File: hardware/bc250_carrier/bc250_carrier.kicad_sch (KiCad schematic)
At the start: 15 parts, among them J1 PSU Mini-Fit Jr 2x5, J10 SENSE, J3 STRIP, J5 FAN1 GPIO5, J6 FAN2 GPIO6, J7 FAN3 GPIO7, J8 FAN4 GPIO10, J9 BTN, Q1 2N7000, U1 ESP32-C3 Super Mini

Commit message: hardware: BC-250 carrier rev C — right-angle PSU header, J11 breakout, wider rails
Rev C relays the 80 x 34.5 mm board around a RIGHT-ANGLE Mini-Fit Jr
(DLL-5569-10AW, C22365658) on the bottom edge: the PSU plug lies flat over a
tracks-only "plug zone" and its wires leave over the top edge.  The 3.3 V
strip feed is a 3 mm track, its return 2.5 mm.  New optional 2x8 breakout
header J11 along the left edge carries 3.3V, 5VSB and 12 V on two pins each
plus every unused GPIO (8, 9, 20, 21, 0) with a ground beside it.  The
button J9 grows to 4 pins (12 V + GND for its ring LED), the sense connector
shrinks to a single pin, the fan headers become a 2 x 2 block spaced for real
fan plugs (Ckmtw W-2510S04P, C140769 — C41927 was a shrouded wafer a fan plug
cannot enter), R1 moves to 7.62 mm pitch, GATE hops layers through two vias.

Every LCSC part number was re-verified against LCSC's product API; MOQs and
pin headers (C2337, C124382) fixed.  `make` now runs KiCad's real DRC through
the pcbnew Python module (drc.py; only the two stock-M3-courtyard overlaps are
tolerated) alongside check.py, and `make preview` renders a quick Pillow PNG.

The J11 rails were then widened so the breakout is good for about 2 A each,
not the 1.3-1.6 A its 0.5-0.6 mm tracks allowed: 12 V 1.2 mm (back layer up
the strip between J11 and the module), 5VSB 1.0 mm (front layer, same strip;
its trunk from the header to the module 1.0 -> 1.5 mm since J11's draw flows
through it), 3.3V 0.9 mm — the most that fits between mounting holes H3/H1 and
the board edge under the 0.25 hole / 0.3 edge rules.  The README gains a
current budget: the fan block's split 12 V feed is ~2.7 A per column, enough
for a fan plus an AIO pump.

Still to confirm on hardware: the PSU pin map, the module's orientation, and
fan plug polarity.
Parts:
- removed J10: SENSE, Connector_JST:JST_XH_B2B-XH-A_1x02_P2.50mm_Vertical, symbol Connector_Generic:Conn_01x02
- removed J9: BTN, Connector_JST:JST_XH_B2B-XH-A_1x02_P2.50mm_Vertical, symbol Connector_Generic:Conn_01x02
- added J10: SENSE, Connector_PinHeader_2.54mm:PinHeader_1x01_P2.54mm_Vertical, symbol Connector_Generic:Conn_01x01
- added J11: PWR+GPIO/GND (optional), Connector_PinHeader_2.54mm:PinHeader_2x08_P2.54mm_Vertical, symbol Connector_Generic:Conn_02x08_Odd_Even
- added J9: BUTTON, Connector_JST:JST_XH_B4B-XH-A_1x04_P2.50mm_Vertical, symbol Connector_Generic:Conn_01x04
- J1: value PSU Mini-Fit Jr 2x5 -> PSU Mini-Fit Jr 2x5 R/A; footprint Connector_Molex:Molex_Mini-Fit_Jr_5566-10A_2x05_P4.20mm_Vertical -> Connector_Molex:Molex_Mini-Fit_Jr_5569-10A2_2x05_P4.20mm_Horizontal
- R1: footprint Resistor_THT:R_Axial_DIN0207_L6.3mm_D2.5mm_P10.16mm_Horizontal -> Resistor_THT:R_Axial_DIN0207_L6.3mm_D2.5mm_P7.62mm_Horizontal
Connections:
- net 12V: now also J11.5 (Pin_5), J11.6 (Pin_6), J9.1 (Pin_1)
- net 5VSB: now also J11.3 (Pin_3), J11.4 (Pin_4)
- net BTN: now also J9.3 (Pin_3)
- net GND: now also J11.11 (Pin_11), J11.13 (Pin_13), J11.15 (Pin_15), J11.7 (Pin_7), J11.9 (Pin_9), J9.2 (Pin_2), J9.4 (Pin_4)
- net SENSE: now also J10.1 (Pin_1)
- net GPIO0: now reaches U1.16 (GPIO0)
- net GPIO0: now also J11.16 (Pin_16)
- net GPIO8: now reaches U1.4 (GPIO8)
- net GPIO8: now also J11.8 (Pin_8)
- net GPIO9: now reaches U1.5 (GPIO9)
- net GPIO9: now also J11.10 (Pin_10)
- net GPIO20: now reaches U1.7 (GPIO20)
- net GPIO20: now also J11.12 (Pin_12)
- net GPIO21: now reaches U1.8 (GPIO21)
- net GPIO21: now also J11.14 (Pin_14)
- net VIN renamed 3.3V
- net 3.3V: now also J11.1 (Pin_1), J11.2 (Pin_2)
- no-connect marks 10 -> 5

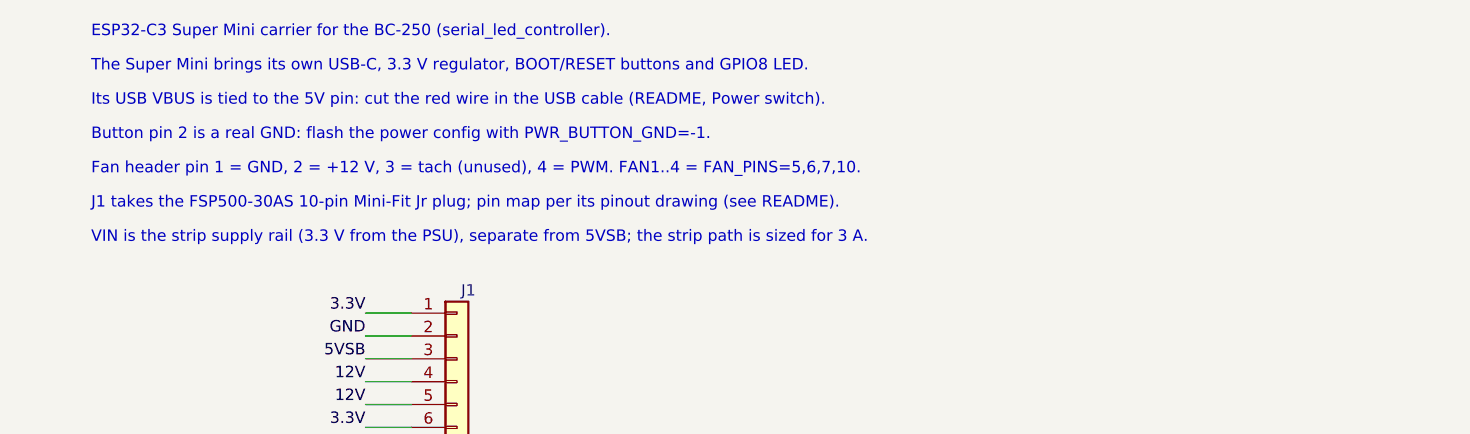
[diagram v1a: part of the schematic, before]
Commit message: hardware: reword two schematic notes that still quoted the retired make variables
The PWR_BUTTON_GND and FAN_PINS variables are gone since v1.18.0/v1.19.0;
the notes now name the config keys (power_switch.pins.button_gnd null,
fans.header1..4 = GPIO 5, 6, 7, 10) and say which J9 pin is the switch
common. Schematic text only — the .kicad_pcb, and so the gerbers already at
the fab, are untouched.
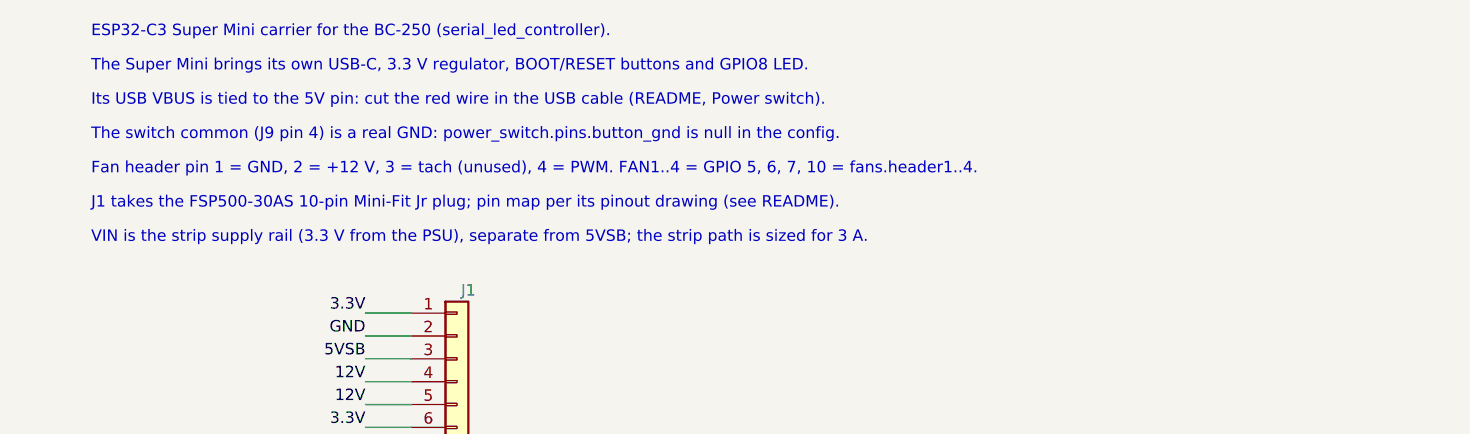
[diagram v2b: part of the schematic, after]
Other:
- note added: "Fan header pin 1 = GND, 2 = +12 V, 3 = tach (unused), 4 = PWM. FAN1..4 = GPIO 5, 6, 7, 10 = fans.header1..4."
- note added: "The switch common (J9 pin 4) is a real GND: power_switch.pins.button_gnd is null in the config."
- note removed: "Button pin 2 is a real GND: flash the power config with PWR_BUTTON_GND=-1."
- note removed: "Fan header pin 1 = GND, 2 = +12 V, 3 = tach (unused), 4 = PWM. FAN1..4 = FAN_PINS=5,6,7,10."
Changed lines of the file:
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@@
     )
   )
-  (text "Button pin 2 is a real GND: flash the power config with PWR_BUTTON_GND=-1."
+  (text "The switch common (J9 pin 4) is a real GND: power_switch.pins.button_gnd is null in the config."
     (at 20.32 31.75 0)
     (effects
@@
     )
   )
-  (text "Fan header pin 1 = GND, 2 = +12 V, 3 = tach (unused), 4 = PWM. FAN1..4 = FAN_PINS=5,6,7,10."
+  (text "Fan header pin 1 = GND, 2 = +12 V, 3 = tach (unused), 4 = PWM. FAN1..4 = GPIO 5, 6, 7, 10 = fans.header1..4."
     (at 20.32 35.56 0)
     (effects

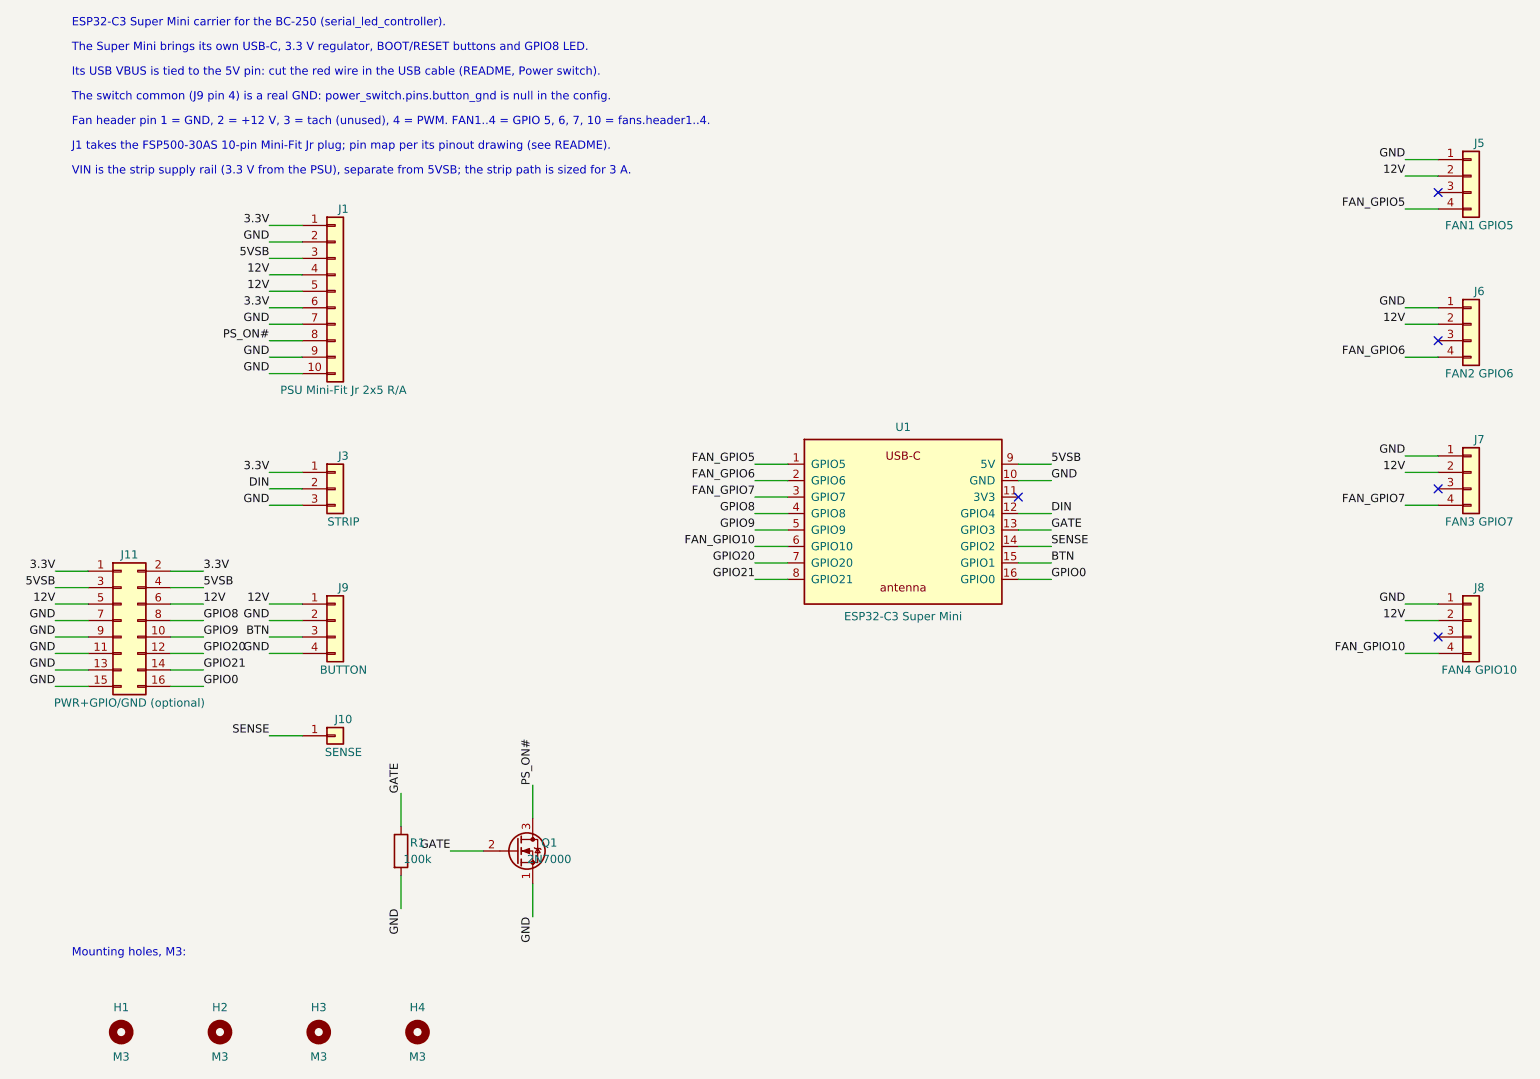
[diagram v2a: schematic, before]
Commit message: carrier pcb: order-ready assembly files per fab, the Super Mini plugs into sockets
fab.py turns the exported gerbers, position file and generate.py's parts
tables into one folder per fab under out/fab/ (JLCPCB, PCBWay): gerber zip,
BOM and pick-and-place in that fab's own column layout, driven by a PROVIDERS
table so another fab is one more entry. `make export` runs it.

The ESP32-C3 Super Mini is no longer soldered: it plugs into two 1x8 5.7 mm
low-profile female headers (J12/J13), so an assembled board from either fab
is complete and the module comes out for reflashing. U1 stays schematic-only.
Fan headers are now the Molex 47053-1000 the 4-wire fan spec names (the
Ckmtw ramp had to be cut for the plug's latch wall), J10/J11 move to stocked
LCSC parts, and the README gains an Ordering section covering assembled and
self-soldered routes.
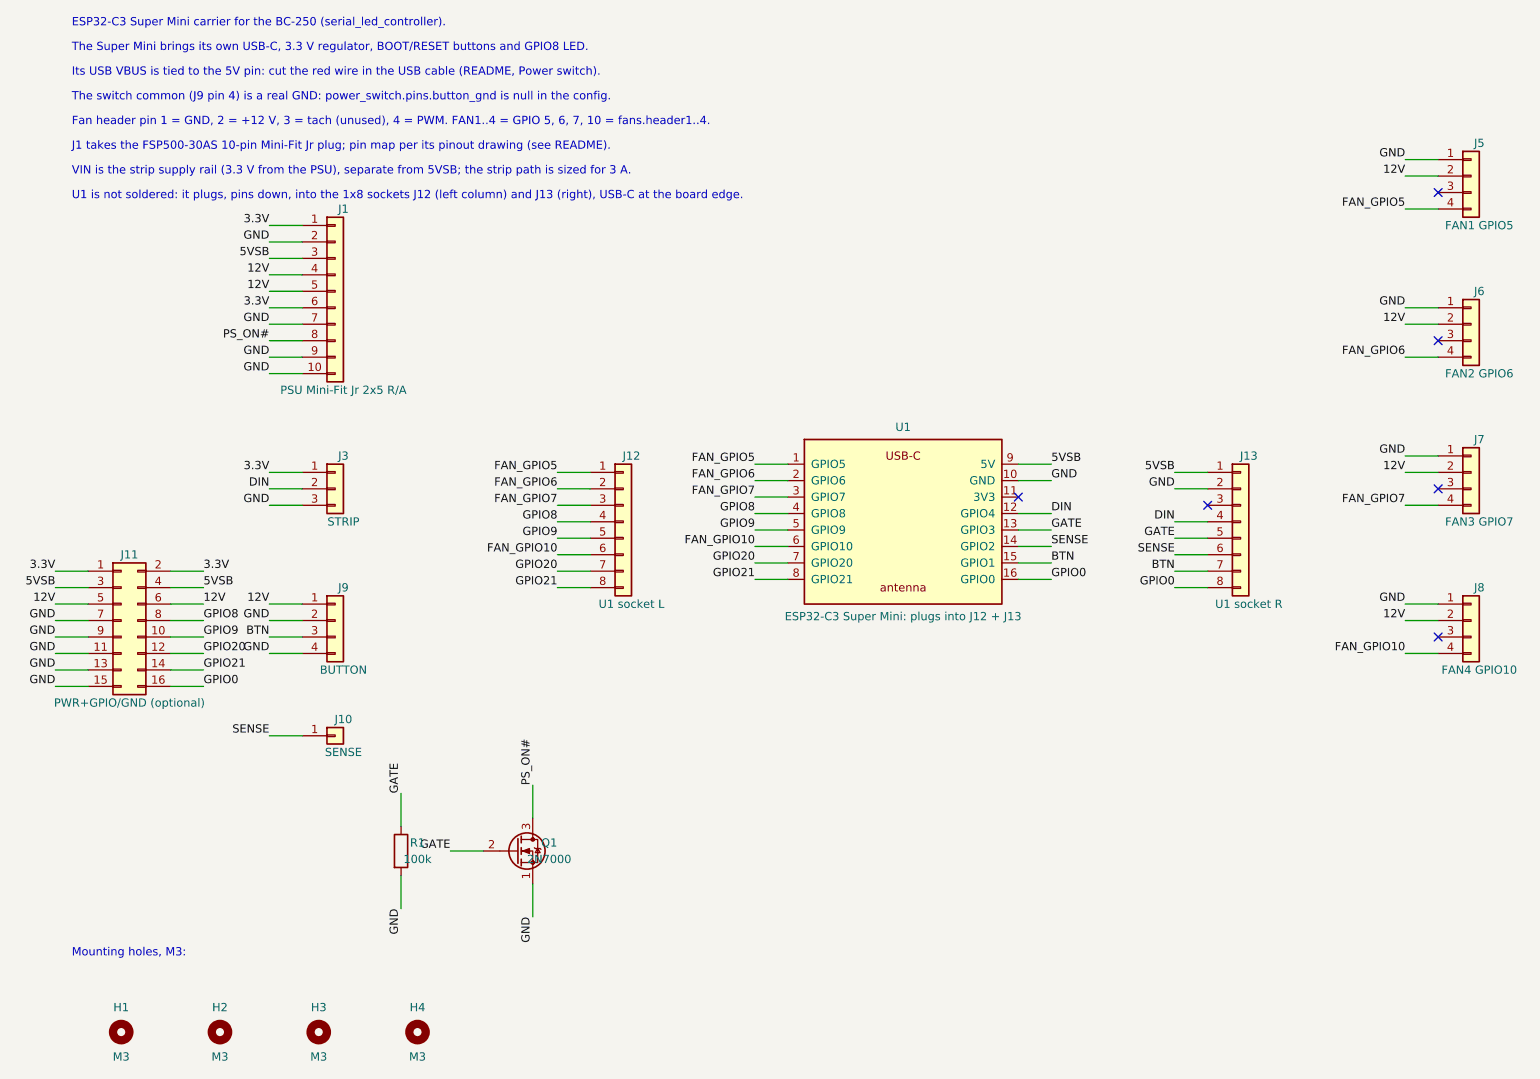
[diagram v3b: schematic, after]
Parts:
- added J12: U1 socket L, Connector_PinSocket_2.54mm:PinSocket_1x08_P2.54mm_Vertical, symbol Connector_Generic:Conn_01x08
- added J13: U1 socket R, Connector_PinSocket_2.54mm:PinSocket_1x08_P2.54mm_Vertical, symbol Connector_Generic:Conn_01x08
- U1: value ESP32-C3 Super Mini -> ESP32-C3 Super Mini: plugs into J12 + J13; footprint bc250_carrier:ESP32-C3_SuperMini -> (none); now left out of the parts list
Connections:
- net 5VSB: now also J13.1 (Pin_1)
- net BTN: now also J13.7 (Pin_7)
- net DIN: now also J13.4 (Pin_4)
- net FAN_GPIO10: now also J12.6 (Pin_6)
- net FAN_GPIO5: now also J12.1 (Pin_1)
- net FAN_GPIO6: now also J12.2 (Pin_2)
- net FAN_GPIO7: now also J12.3 (Pin_3)
- net GATE: now also J13.5 (Pin_5)
- net GND: now also J13.2 (Pin_2)
- net GPIO0: now also J13.8 (Pin_8)
- net GPIO20: now also J12.7 (Pin_7)
- net GPIO21: now also J12.8 (Pin_8)
- net GPIO8: now also J12.4 (Pin_4)
- net GPIO9: now also J12.5 (Pin_5)
- net SENSE: now also J13.6 (Pin_6)
- no-connect marks 5 -> 6
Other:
- note added: "U1 is not soldered: it plugs, pins down, into the 1x8 sockets J12 (left column) and J13 (right), USB-C at the board edge."

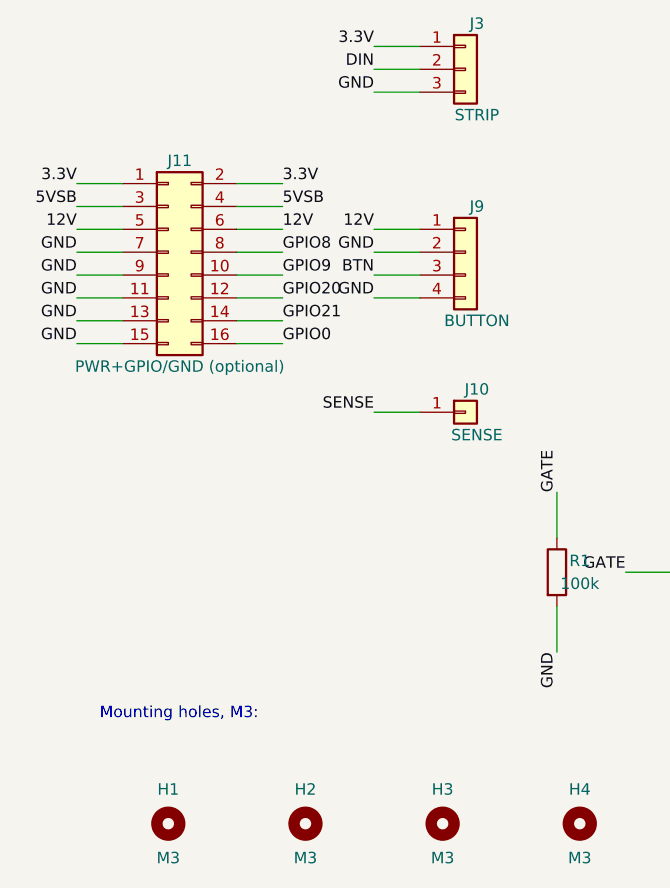
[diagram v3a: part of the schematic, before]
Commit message: carrier pcb rev D: 0.5 mm hand-solder clearances, wide TO-92, rails split from the GPIOs
Board 2's fault was PS_ON# bridged to GATE at the stock TO-92's 0.3 mm
gate-drain gap; Q1 is now on the wide footprint. check.py holds tracks
0.5 mm from any other part's pad (0.3 track to track), and on the back
12 V passes no 5VSB, GATE or GPIO pad. J11 becomes a 2x6 of SENSE + the
spare GPIOs with GND beside each; the rails move to their own 2x3 J14.
Both layers get a ground fill (fill.py: KiCad's zone filler + stitching
vias).
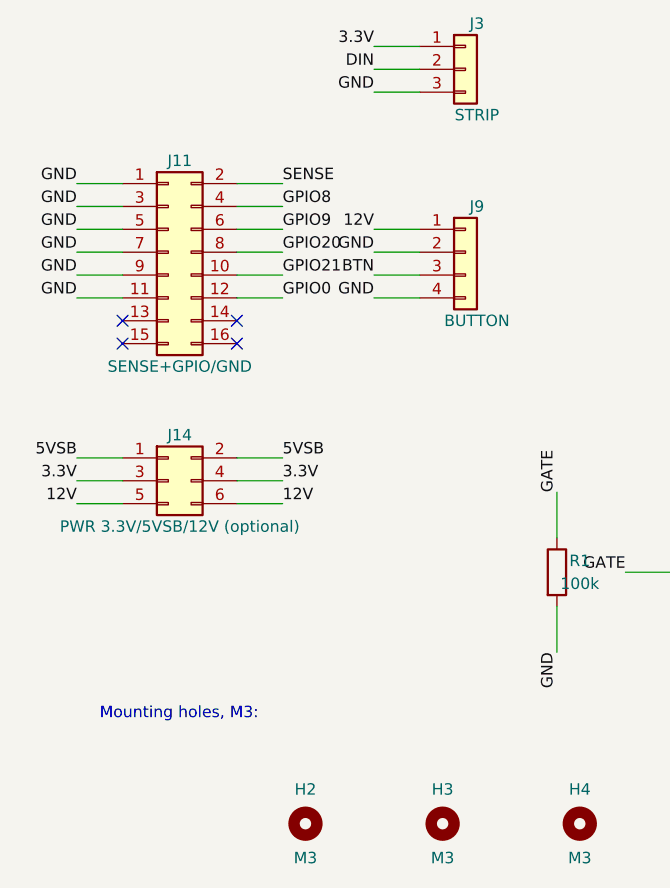
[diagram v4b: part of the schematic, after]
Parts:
- removed H1: M3, MountingHole:MountingHole_3.2mm_M3, symbol Mechanical:MountingHole
- removed J10: SENSE, Connector_PinHeader_2.54mm:PinHeader_1x01_P2.54mm_Vertical, symbol Connector_Generic:Conn_01x01
- added J14: PWR 3.3V/5VSB/12V (optional), Connector_PinHeader_2.54mm:PinHeader_2x03_P2.54mm_Vertical, symbol Connector_Generic:Conn_02x03_Odd_Even
- J11: value PWR+GPIO/GND (optional) -> SENSE+GPIO/GND; footprint Connector_PinHeader_2.54mm:PinHeader_2x08_P2.54mm_Vertical -> Connector_PinHeader_2.54mm:PinHeader_2x06_P2.54mm_Vertical
- Q1: footprint Package_TO_SOT_THT:TO-92_Inline -> Package_TO_SOT_THT:TO-92_Inline_Wide
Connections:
- net 12V: now also J14.5 (Pin_5), J14.6 (Pin_6); no longer J11.5 (Pin_5), J11.6 (Pin_6)
- net 3.3V: now also J14.3 (Pin_3), J14.4 (Pin_4); no longer J11.1 (Pin_1), J11.2 (Pin_2)
- net 5VSB: now also J14.1 (Pin_1), J14.2 (Pin_2); no longer J11.3 (Pin_3), J11.4 (Pin_4)
- net GND: now also J11.1 (Pin_1), J11.3 (Pin_3), J11.5 (Pin_5); no longer J11.13 (Pin_13), J11.15 (Pin_15)
- net GPIO0: now also J11.12 (Pin_12); no longer J11.16 (Pin_16)
- net GPIO20: now also J11.8 (Pin_8); no longer J11.12 (Pin_12)
- net GPIO21: now also J11.10 (Pin_10); no longer J11.14 (Pin_14)
- net GPIO8: now also J11.4 (Pin_4); no longer J11.8 (Pin_8)
- net GPIO9: now also J11.6 (Pin_6); no longer J11.10 (Pin_10)
- net SENSE: now also J11.2 (Pin_2)
- no-connect marks 6 -> 10
